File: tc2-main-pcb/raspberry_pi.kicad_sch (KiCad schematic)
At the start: 22 parts, among them J1 Screw_Terminal_01x01, J4 Raspberry_Pi_2_3, J5 Screw_Terminal_01x01, J6 Screw_Terminal_01x01, U13 MAX98357, U14 SPH0645LM4H, U15 ME6211

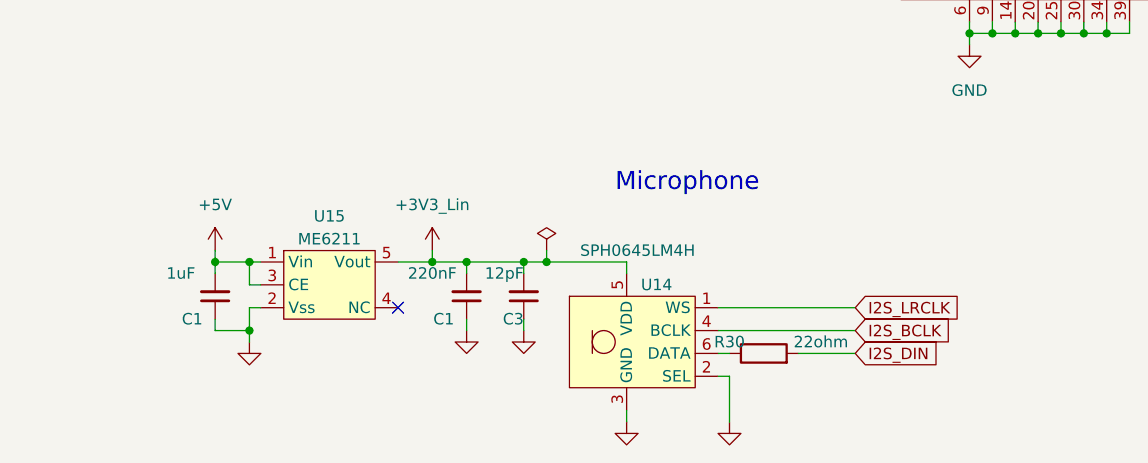
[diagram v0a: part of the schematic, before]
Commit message: Clean up of files and updated drawings for PCBs
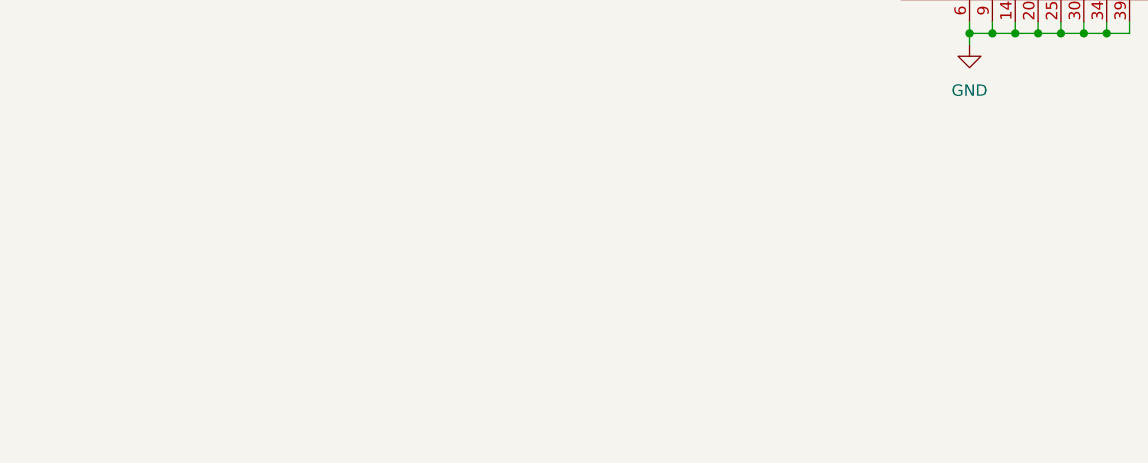
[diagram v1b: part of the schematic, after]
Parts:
- removed C1: 220nF, Capacitor_SMD:C_0402_1005Metric, symbol Device:C_Small
- removed C1: 1uF, Capacitor_SMD:C_0402_1005Metric, symbol Device:C_Small
- removed C3: 12pF, Capacitor_SMD:C_0402_1005Metric, symbol Device:C_Small
- removed R30: 22ohm, Resistor_SMD:R_0402_1005Metric, symbol Device:R
- removed U14: SPH0645LM4H, cacophony-library:MIC_SPH0645LM4H-B, symbol cacophony-library:SPH0645LM4H
- removed U15: ME6211, Package_TO_SOT_SMD:SOT-23-5, symbol cacophony-library:ME6211
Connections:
- no-connect marks 18 -> 17
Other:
- note removed: "Microphone"

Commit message: Version 2 WIP
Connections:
- net ~{WAKEUP_PING}: now reaches J4.36 (GPIO16)
- net I2S_DIN: no longer names the net of J4.38 (GPIO20/MOSI1)
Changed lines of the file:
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@@
   (no_connect (at 121.92 124.46))
   (no_connect (at 162.56 124.46))
-  (no_connect (at 121.92 91.44))
   (no_connect (at 55.88 62.23))
   (no_connect (at 190.5 95.25))
@@
   (no_connect (at 50.8 62.23))
   (no_connect (at 162.56 127))
+  (no_connect (at 121.92 104.14))
   (no_connect (at 53.34 62.23))
   (no_connect (at 190.5 100.33))
@@
     (stroke (width 0) (type default))
   )
+  (wire (pts (xy 120.65 91.44) (xy 121.92 91.44))
+    (stroke (width 0) (type default))
+  )
   (wire (pts (xy 59.69 29.21) (xy 59.69 36.83))
     (stroke (width 0) (type default))
@@
   )
   (wire (pts (xy 162.56 114.3) (xy 196.85 114.3))
-    (stroke (width 0) (type default))
-  )
-  (wire (pts (xy 100.33 104.14) (xy 121.92 104.14))
     (stroke (width 0) (type default))
   )
@@
     (effects (font (size 1.27 1.27)) (justify left bottom))
   )
-  (label "RPI_SPI_MISO_" (at 165.1 114.3 0) (fields_autoplaced)
-    (effects (font (size 1.27 1.27)) (justify left bottom))
-  )
   (label "RPI_SPI_MOSI_" (at 165.1 116.84 0) (fields_autoplaced)
     (effects (font (size 1.27 1.27)) (justify left bottom))
   )
-  (global_label "I2S_DIN" (shape input) (at 100.33 104.14 180) (fields_autoplaced)
-    (effects (font (size 1.27 1.27)) (justify right))
-    (property "Intersheetrefs" "${INTERSHEET_REFS}" (at 90.2275 104.14 0)
-      (effects (font (size 1.27 1.27)) (justify right) hide)
-    )
-  )
   (global_label "RPI_SPI_SCLK" (shape input) (at 196.85 119.38 0) (fields_autoplaced)
     (effects (font (size 1.27 1.27)) (justify left))
@@
     )
   )
+  (global_label "~{WAKEUP_PING}" (shape input) (at 120.65 91.44 180) (fields_autoplaced)
+    (effects (font (size 1.27 1.27)) (justify right))
+    (property "Intersheetrefs" "${INTERSHEET_REFS}" (at 104.7418 91.44 0)
+      (effects (font (size 1.27 1.27)) (justify right) hide)
+    )
+  )

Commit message: Thermal camera V2 WIP
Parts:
- removed C38: 10uF, Capacitor_SMD:C_0603_1608Metric, symbol Device:C_Small
- removed C39: 220nF, Capacitor_SMD:C_0402_1005Metric, symbol Device:C_Small
- removed R29: 100k, Resistor_SMD:R_0402_1005Metric, symbol Device:R
- removed U13: MAX98357, Package_DFN_QFN:TQFN-16-1EP_3x3mm_P0.5mm_EP1.6x1.6mm, symbol cacophony-library:MAX98357
- added C1: 220nF, Capacitor_SMD:C_0402_1005Metric, symbol Device:C_Small
- added C35: 10uF, Capacitor_SMD:C_0603_1608Metric, symbol Device:C_Small
- added U14: MAX98357AEWL+T, cacophony-library:WLP-9_L1.4-W1.3-P0.40-R3-C3-BR, symbol cacophony-library:MAX98357AEWL+T
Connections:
- net +5V: now also C1.2, C35.1, U14.A2 (VDD)
- net GND: now also C1.1, C35.2, U14.B2 (GAIN_SLOT), U14.C2 (GND)
- net I2S_BCLK: now also U14.C1 (BCLK)
- net I2S_DOUT: now also U14.B1 (DIN)
- net I2S_LRCLK: now also U14.C3 (LRCLK)
- net SPEAKER_+: now also U14.A3 (OUTP)
- net SPEAKER_-: now also U14.B3 (OUTN)
- net at R28.2: now also U14.A1 (~{SD_MODE})
- no-connect marks 17 -> 13
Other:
- moved on the sheet: R28

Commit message: P2 milestone
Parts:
- removed R15: 1k, Resistor_SMD:R_0402_1005Metric, symbol Device:R
- added C18: 10uF, Capacitor_SMD:C_0603_1608Metric, symbol Device:C_Small
- added J8: Screw_Terminal_01x01, cacophony-library:SMTSO25, symbol Connector:Screw_Terminal_01x01
- added R1: 1k, Resistor_SMD:R_0402_1005Metric, symbol Device:R
- added U15: 74HC4052, cacophony-library:SOP-16_L10.0-W3.9-P1.27-LS6.0-BL, symbol cacophony-library:74HC4052
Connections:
- net +5V: now also C18.1, U15.16 (VDD)
- net ATtiny_RESET_UPDI: now also U15.1 (2Y0), U15.12 (1Y0); no longer J4.10 (GPIO15/RXD)
- net GND: now also C18.2, U15.6 (~{E}), U15.7 (VEE), U15.8 (GND)
- net at J4.8 (GPIO14/TXD): now also R1.1
- net ~{PI_SHUTDOWN}: now reaches J4.13 (GPIO27)
- net MUL_S0: now reaches J4.31 (GCLK2/GPIO6)
- net MUL_S0: now also U15.10 (S0)
- net MUL_S1: now reaches J4.32 (PWM0/GPIO12)
- net MUL_S1: now also U15.9 (S1)
- new net ATTINY_RX: U15.2 (2Y2)
- new net ATTINY_TX: U15.15 (1Y2)
- new net OUT_RX: U15.14 (1Y1)
- new net OUT_TX: U15.5 (2Y1)
- new net RPI_RX: J4.10 (GPIO15/RXD), U15.13 (1Z)
- new net RPI_TX: R1.2, U15.3 (2Z)
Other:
- moved on the sheet: J1, J4, J5, J6, R14, R29, R30, R31, R32, R34

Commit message: P3-Nov release
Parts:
- added C1: 220nF, Capacitor_SMD:C_0402_1005Metric, symbol Device:C_Small
- added J2: Screw_Terminal_01x01, cacophony-library:SMTSO25, symbol Connector:Screw_Terminal_01x01
- added U17: PCA9515ADP,118, Package_SO:TSSOP-8_3x3mm_P0.65mm, symbol cacophony-library:PCA9515ADP,118
- J4: footprint cacophony-library:RPI_HDR-SMD_40P-P2.54-V-F-R2-C20-S8.7-EH -> cacophony-library:HDR-SMD_40P-P2.54-V-F-R2-C20-LS8.2-EH; LCSC C2685111 -> C2685098
- U15: footprint cacophony-library:SOP-16_L10.0-W3.9-P1.27-LS6.0-BL -> Package_SO:SOP-16_3.9x9.9mm_P1.27mm
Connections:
- net GND: now also C1.1, U17.4 (GND)
- net SCL: now also U17.2 (SCL0); no longer J4.5 (SCL/GPIO3)
- net SDA: now also U17.3 (SDA0); no longer J4.3 (SDA/GPIO2)
- net ~{PI_SHUTDOWN}: now also J4.37 (GPIO26); no longer J4.13 (GPIO27)
- net MODEM_POWER_EN: now reaches J4.38 (GPIO20/MOSI1)
- net ATTINY_RX: no longer names the net of U15.2 (2Y2)
- net ATTINY_TX: no longer names the net of U15.15 (1Y2)
- net ~{WAKEUP_PING} renamed ~{READ_ATTINY_CMD_REG}
- new net +3V3: C1.2, U17.8 (VCC)
- new net 5V_EN: U17.5 (EN)
- new net RPI_SCL: J4.5 (SCL/GPIO3), U17.7 (SCL1)
- new net RPI_SDA: J4.3 (SDA/GPIO2), U17.6 (SDA1)
- new net ~{PI_POWERED_OFF}: J4.13 (GPIO27)
- no-connect marks 13 -> 15

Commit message: v0.4.0
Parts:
- removed U17: PCA9515ADP,118, Package_SO:TSSOP-8_3x3mm_P0.65mm, symbol cacophony-library:PCA9515ADP,118
- added R41, R47, R52: 100k, Resistor_SMD:R_0402_1005Metric, symbol Device:R
- added TP11, TP15, TP16, TP21, TP22, TP7: TestPoint, cacophony-library:TP, symbol Connector:TestPoint
- added U18: TCA4311ADGKR, Package_SO:MSOP-8_3x3mm_P0.65mm, symbol cacophony-library:TCA4311ADGKR
- J1, J2, J5, J6, J8: footprint cacophony-library:SMTSO25 -> cacophony-library:smd_nut_SMTSO25
- J4: symbol Connector:Raspberry_Pi_2_3 -> cacophony-library:Raspberry_Pi_2_3
- U14: LCSC (none) -> C2682619; LCSC Part C2682619 -> (none)
- U15: LCSC (none) -> C111594; LCSC Part C111594 -> (none)
- renumbered C35 to C28, C1 to C29, C18 to C37, C1 to C50, R28 to R12, R1 to R37
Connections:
- net +3V3: now also C37.1, U15.16 (VDD), U18.8 (VCC)
- net +5V: no longer C37.1, U15.16 (VDD)
- net 5V_EN: now also U18.1 (EN)
- net GND: now also R41.1, R47.1, R52.1, U18.4 (GND); no longer U15.6 (~{E})
- net RPI_SCL: now also U18.3 (SCLIN)
- net RPI_SDA: now also U18.6 (SDAIN)
- net SCL: now also U18.2 (SCLOUT)
- net SDA: now also U18.7 (SDAOUT)
- net I2C_BUS_LOCK: now reaches J4.33 (PWM1/GPIO13)
- net at U15.11 (1Y3): now also TP11.1
- net at U15.15 (1Y2): now also TP15.1
- net at U15.2 (2Y2): now also TP16.1
- net at U15.4 (2Y3): now also TP21.1
- net MUL_S1: no longer names the net of U15.9 (S1)
- net MUL_S1: now also R47.2, TP7.1; no longer J4.32 (PWM0/GPIO12)
- new net: R52.2, U18.5 (READY)
- new net GPIO12: J4.32 (PWM0/GPIO12), TP22.1
- new net ~{UART_MULTIPLEX_EN}: R41.2, U15.6 (~{E})
- no-connect marks 15 -> 9
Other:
- moved on the sheet: C37, C50, J1, J2, J5, J6, J8, U15

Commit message: Adding panel
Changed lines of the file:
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@@
+		)
+	)
+	(text_box "Search 2x20p 8.5 for finding a through hole replacement for the connector\nC350295\nC429949\nC169819"
+		(exclude_from_sim no)
+		(at 111.76 77.47 0)
+		(size 31.75 13.97)
+		(stroke
+			(width 0)
+			(type default)
+		)
+		(fill
+			(type none)
+		)
+		(effects
+			(font
+				(size 1.27 1.27)
+			)
+			(justify left top)
 		)
 	)
